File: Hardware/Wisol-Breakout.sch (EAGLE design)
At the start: 13 parts

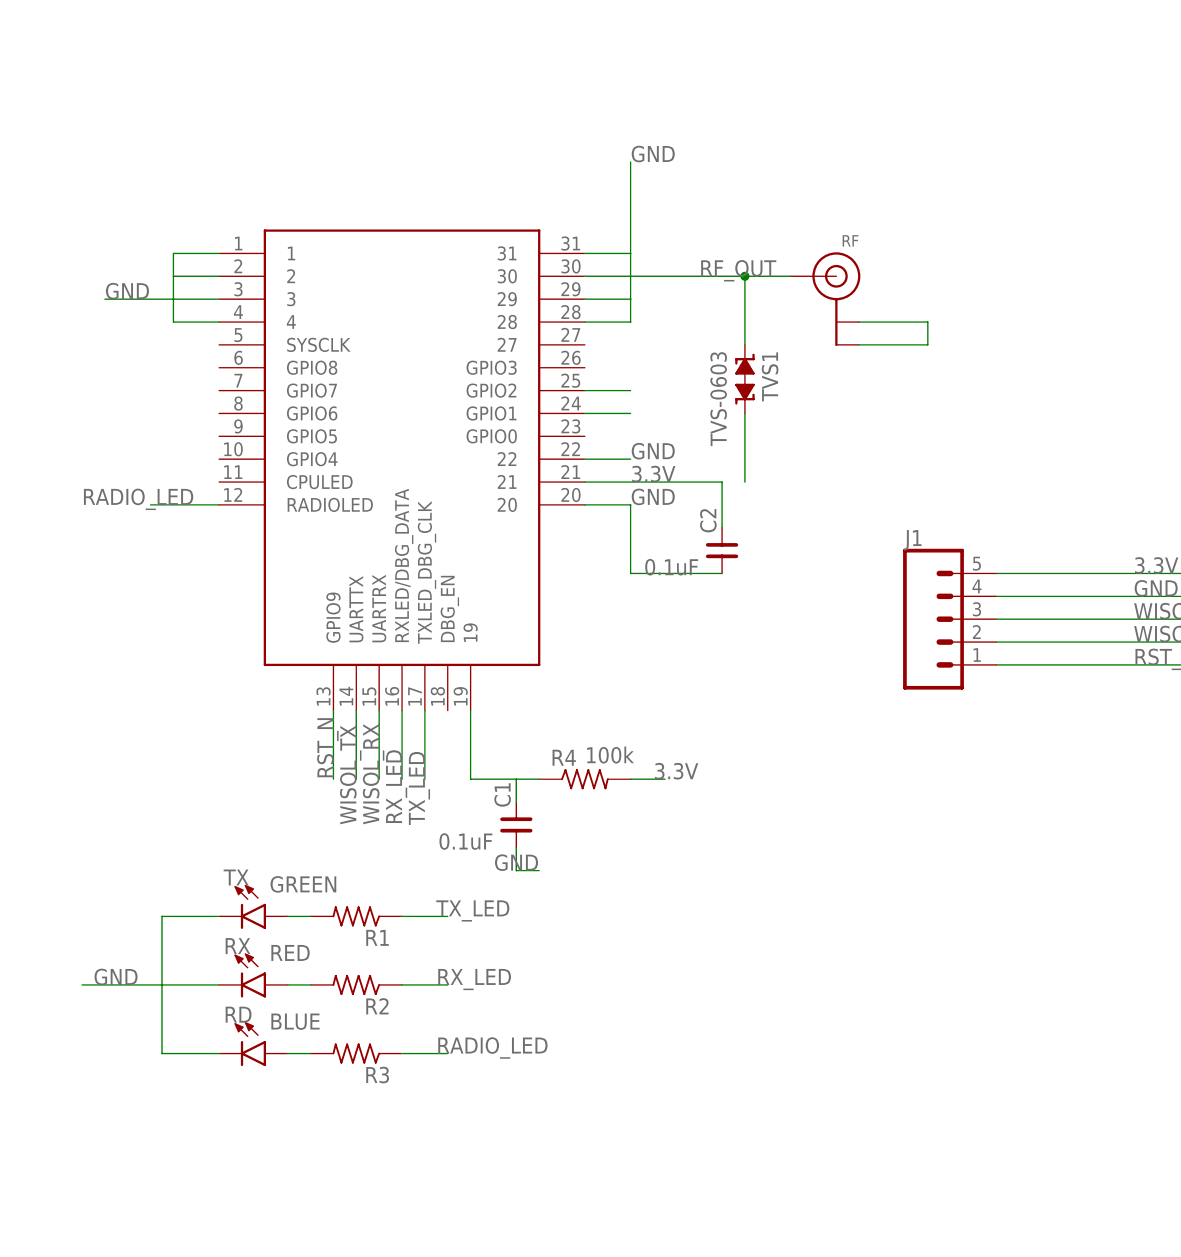
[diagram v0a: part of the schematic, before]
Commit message: Updated for Seeed PCB Assembly
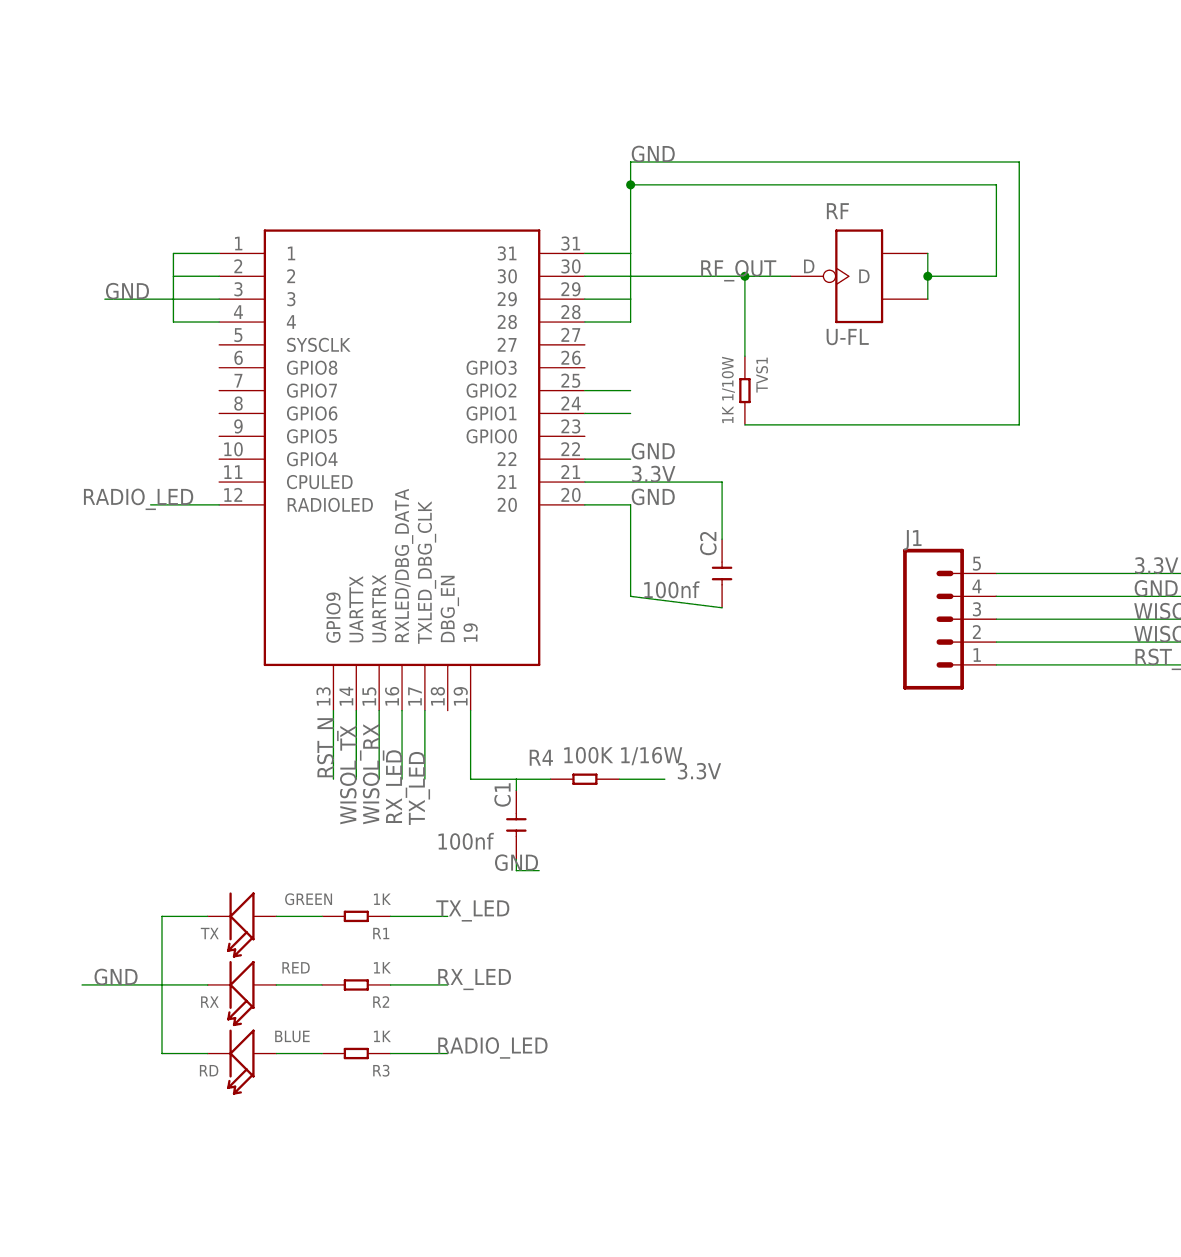
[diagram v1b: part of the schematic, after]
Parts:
- removed WSSFM10R2: WSSFM10R2/R4WSSFM10R2R4, SigfoxMod-RCZ1:WSSFM10R2/R4WSSFM10R2R4
- added WSSFM10R: WSSFM10RWSSFM10R2R4, WisolWSSFM10R:WSSFM10RWSSFM10R2R4
- C1, C2: value 0.1uF -> 100nf; device IoTthings:CNP-0402 -> Seeed-Capacitor:CERAMIC-100NF-25V-10%-X7R(0402)
- R1, R2, R3: value (none) -> 1K; device IoTthings:R-US_R0402 -> Seeed-Resistor:SMD-RES-1K-5%-1/16W(0402); MPN (none) -> RC0402FR-071KL
- R4: value 100k -> 100K 1/16W; device IoTthings:R-US_R0402 -> Seeed-Resistor:SMD-RES-100K-5%-1/16W(0402)
- RD: device IoTthings:LED-BLUE0603 -> Seeed-LED:SMD-LED-CLEAR-BLUE(0603)
- RF: value (none) -> U-FL; device IoTthings:ANTENNA_U.FL -> Seeed-Connector:ANTENNA-CONN-U-FL(3P)
- RX: device IoTthings:LED-RED0603 -> Seeed-LED:LED-SMD-RED-DIFFUSED(0603)
- TVS1: value TVS-0603 -> 1K 1/10W; device supressor:TVS-0603 -> Seeed-Fuse:SMD-ESD-CG0603MLC-05E
- TX: device IoTthings:LED-GREEN0603 -> Seeed-LED:SMD-LED-CLEAR-GREEN(0603)
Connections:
- net 3.3V: now also WSSFM10R.21; no longer WSSFM10R2.21
- net GND: now also RD.-, RF.GND1, RF.GND2, RX.-, TX.-, WSSFM10R.1, WSSFM10R.2, WSSFM10R.20, WSSFM10R.22, WSSFM10R.28, WSSFM10R.29, WSSFM10R.3, WSSFM10R.31, WSSFM10R.4; no longer RD.C, RF.GND@0, RF.GND@1, RX.C, TX.C, WSSFM10R2.1, WSSFM10R2.2, WSSFM10R2.20, WSSFM10R2.22, WSSFM10R2.28, WSSFM10R2.29, WSSFM10R2.3, WSSFM10R2.31, WSSFM10R2.4
- net GPIO1: now also WSSFM10R.GPIO1; no longer WSSFM10R2.GPIO1
- net GPIO2: now also WSSFM10R.GPIO2; no longer WSSFM10R2.GPIO2
- net N$1: now also WSSFM10R.19; no longer WSSFM10R2.19
- net N$2: now also TX.+; no longer TX.A
- net N$3: now also RX.+; no longer RX.A
- net N$4: now also RD.+; no longer RD.A
- net RADIO_LED: now also WSSFM10R.RADIOLED; no longer WSSFM10R2.RADIOLED
- net RF_OUT: now also RF.D, WSSFM10R.30; no longer RF.SIGNAL, WSSFM10R2.30
- net RST_N: now also WSSFM10R.GPIO9; no longer WSSFM10R2.GPIO9
- net RX_LED: now also WSSFM10R.RXLED/DBG_DATA; no longer WSSFM10R2.RXLED/DBG_DATA
- net TX_LED: now also WSSFM10R.TXLED_DBG_CLK; no longer WSSFM10R2.TXLED_DBG_CLK
- net WISOL_RX: now also WSSFM10R.UARTRX; no longer WSSFM10R2.UARTRX
- net WISOL_TX: now also WSSFM10R.UARTTX; no longer WSSFM10R2.UARTTX

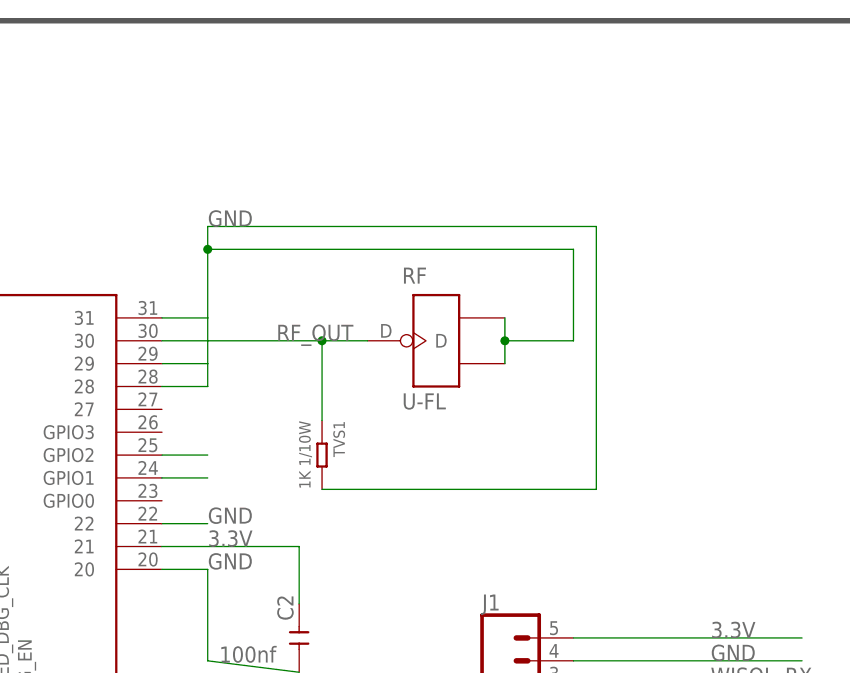
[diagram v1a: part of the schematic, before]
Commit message: Added RF inductor as recommended by Wisol H/W Design Guide
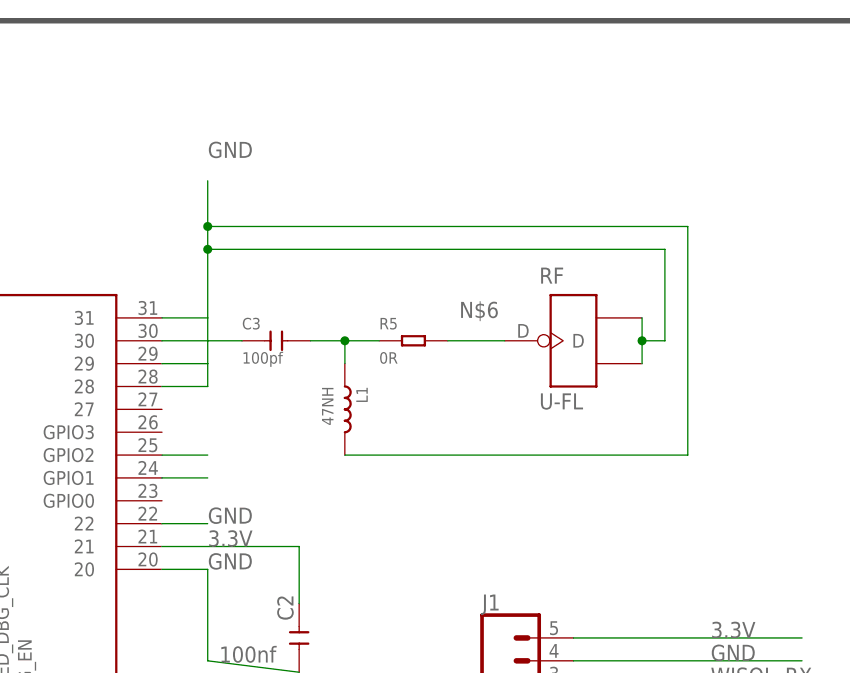
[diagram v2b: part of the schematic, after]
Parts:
- removed TVS1: 1K 1/10W, Seeed-Fuse:SMD-ESD-CG0603MLC-05E
- added C3: 100pf, Seeed-Capacitor:CERAMIC-100PF-50V-5%-NPO(0402)
- added L1: 47NH, Seeed-Inductor:SMD-INDUCTOR-15NH-5%-300MA(0402)
- added R5: 0R, Seeed-Resistor:SMD-RES-0R-5%-1/16W(0402)
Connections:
- new net N$5: C3.2, L1.1, R5.1
- new net N$6: R5.2, RF.D
- net GND: now also L1.2; no longer TVS1.2
- net RF_OUT: now also C3.1; no longer RF.D, TVS1.1
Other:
- moved on the sheet: RF
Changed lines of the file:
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@@
 <layer number="136" name="silktop" color="7" fill="1" visible="yes" active="yes"/>
 <layer number="137" name="silkbottom" color="7" fill="1" visible="yes" active="yes"/>
+<layer number="138" name="mbTest" color="7" fill="1" visible="yes" active="yes"/>
+<layer number="139" name="mtKeepout" color="7" fill="1" visible="yes" active="yes"/>
+<layer number="140" name="mbKeepout" color="7" fill="1" visible="yes" active="yes"/>
+<layer number="141" name="mtRestrict" color="7" fill="1" visible="yes" active="yes"/>
+<layer number="142" name="mbRestrict" color="7" fill="1" visible="yes" active="yes"/>
+<layer number="143" name="mvRestrict" color="7" fill="1" visible="yes" active="yes"/>
 <layer number="144" name="Drill_legend" color="7" fill="1" visible="yes" active="yes"/>
 <layer number="145" name="DrillLegend_01-16" color="7" fill="1" visible="yes" active="yes"/>
 <layer number="146" name="DrillLegend_01-20" color="7" fill="1" visible="yes" active="yes"/>
+<layer number="147" name="mMeasures" color="7" fill="1" visible="yes" active="yes"/>
+<layer number="148" name="mDocument" color="7" fill="1" visible="yes" active="yes"/>
+<layer number="149" name="mReference" color="7" fill="1" visible="yes" active="yes"/>
 <layer number="150" name="Notes" color="7" fill="1" visible="no" active="yes"/>
 <layer number="151" name="HeatSink" color="7" fill="1" visible="yes" active="yes"/>
@@
 <layer number="166" name="AntennaArea" color="7" fill="1" visible="yes" active="yes"/>
 <layer number="168" name="4mmHeightArea" color="7" fill="1" visible="yes" active="yes"/>
+<layer number="191" name="mNets" color="7" fill="1" visible="yes" active="yes"/>
+<layer number="192" name="mBusses" color="7" fill="1" visible="yes" active="yes"/>
+<layer number="193" name="mPins" color="7" fill="1" visible="yes" active="yes"/>
+<layer number="194" name="mSymbols" color="7" fill="1" visible="yes" active="yes"/>
+<layer number="195" name="mNames" color="7" fill="1" visible="yes" active="yes"/>
+<layer number="196" name="mValues" color="7" fill="1" visible="yes" active="yes"/>
 <layer number="199" name="Contour" color="7" fill="1" visible="no" active="yes"/>
 <layer number="200" name="200bmp" color="7" fill="1" visible="yes" active="yes"/>
@@
 <part name="R4" library="Seeed-Resistor" library_urn="urn:adsk.eagle:library:474" deviceset="SMD-RES-100K-5%-1/16W(0402)" device="" package3d_urn="urn:adsk.eagle:package:32792/1" value="100K 1/16W"/>
 <part name="C1" library="Seeed-Capacitor" library_urn="urn:adsk.eagle:library:464" deviceset="CERAMIC-100NF-25V-10%-X7R(0402)" device="" package3d_urn="urn:adsk.eagle:package:32379/1" value="100nf"/>
-<part name="TVS1" library="Seeed-Fuse" library_urn="urn:adsk.eagle:library:469" deviceset="SMD-ESD-CG0603MLC-05E" device="" package3d_urn="urn:adsk.eagle:package:32546/1" value="1K 1/10W"/>
 <part name="C2" library="Seeed-Capacitor" library_urn="urn:adsk.eagle:library:464" deviceset="CERAMIC-100NF-25V-10%-X7R(0402)" device="" package3d_urn="urn:adsk.eagle:package:32379/1" value="100nf"/>
 <part name="J1" library="SparkFun-Connectors" deviceset="CONN_05" device=""/>
@@
 <part name="TX" library="Seeed-LED" library_urn="urn:adsk.eagle:library:472" deviceset="SMD-LED-CLEAR-GREEN(0603)" device="" package3d_urn="urn:adsk.eagle:package:32743/1" value="GREEN"/>
 <part name="RF" library="Seeed-Connector" library_urn="urn:adsk.eagle:library:478" deviceset="ANTENNA-CONN-U-FL(3P)" device="" package3d_urn="urn:adsk.eagle:package:33122/1" value="U-FL"/>
+<part name="L1" library="Seeed-Inductor" deviceset="SMD-INDUCTOR-15NH-5%-300MA(0402)" device="" value="47NH">
+<attribute name="MPN" value="LQW15AN47NJ00D"/>
+</part>
+<part name="C3" library="Seeed-Capacitor" deviceset="CERAMIC-100PF-50V-5%-NPO(0402)" device="" value="100pf"/>
+<part name="R5" library="Seeed-Resistor" deviceset="SMD-RES-0R-5%-1/16W(0402)" device="" value="0R"/>
 </parts>
 <sheets>
@@
 <attribute name="VALUE" x="111.76" y="65.0875" size="1.778" layer="96" rot="R180"/>
 </instance>
-<instance part="TVS1" gate="G$1" x="139.7" y="114.3" rot="R270"/>
 <instance part="C2" gate="G$1" x="137.16" y="93.98" smashed="yes" rot="R90">
 <attribute name="NAME" x="136.525" y="95.885" size="1.778" layer="95" rot="R90"/>
@@
 <attribute name="VALUE" x="93.98" y="58.42" size="1.27" layer="96" ratio="10" rot="R180"/>
 </instance>
-<instance part="RF" gate="G$1" x="152.4" y="127"/>
+<instance part="RF" gate="G$1" x="167.64" y="127"/>
+<instance part="L1" gate="G$1" x="142.24" y="119.38" rot="R270"/>
+<instance part="C3" gate="G$1" x="134.62" y="127"/>
+<instance part="R5" gate="G$1" x="149.86" y="127"/>
 </instances>
 <busses>
@@
 <wire x1="127" y1="121.92" x2="127" y2="124.46" width="0.1524" layer="91"/>
 <wire x1="127" y1="129.54" x2="127" y2="137.16" width="0.1524" layer="91"/>
-<label x="127" y="139.7" size="1.778" layer="95"/>
+<label x="127" y="147.32" size="1.778" layer="95"/>
 <pinref part="RF" gate="G$1" pin="GND1"/>
 <pinref part="RF" gate="G$1" pin="GND2"/>
 <wire x1="127" y1="137.16" x2="127" y2="139.7" width="0.1524" layer="91"/>
-<wire x1="160.02" y1="129.54" x2="160.02" y2="127" width="0.1524" layer="91"/>
-<wire x1="160.02" y1="127" x2="160.02" y2="124.46" width="0.1524" layer="91"/>
-<wire x1="160.02" y1="127" x2="167.64" y2="127" width="0.1524" layer="91"/>
-<junction x="160.02" y="127"/>
-<wire x1="167.64" y1="127" x2="167.64" y2="137.16" width="0.1524" layer="91"/>
-<wire x1="167.64" y1="137.16" x2="127" y2="137.16" width="0.1524" layer="91"/>
+<wire x1="127" y1="139.7" x2="127" y2="144.78" width="0.1524" layer="91"/>
+<wire x1="175.26" y1="129.54" x2="175.26" y2="127" width="0.1524" layer="91"/>
+<wire x1="175.26" y1="127" x2="175.26" y2="124.46" width="0.1524" layer="91"/>
+<wire x1="175.26" y1="127" x2="177.8" y2="127" width="0.1524" layer="91"/>
+<junction x="175.26" y="127"/>
+<wire x1="177.8" y1="127" x2="177.8" y2="137.16" width="0.1524" layer="91"/>
+<wire x1="177.8" y1="137.16" x2="127" y2="137.16" width="0.1524" layer="91"/>
 <junction x="127" y="137.16"/>
-<pinref part="TVS1" gate="G$1" pin="2"/>
-<wire x1="139.7" y1="110.49" x2="170.18" y2="110.49" width="0.1524" layer="91"/>
-<wire x1="170.18" y1="110.49" x2="170.18" y2="139.7" width="0.1524" layer="91"/>
-<wire x1="170.18" y1="139.7" x2="127" y2="139.7" width="0.1524" layer="91"/>
+<pinref part="L1" gate="G$1" pin="2"/>
+<wire x1="142.24" y1="114.3" x2="180.34" y2="114.3" width="0.1524" layer="91"/>
+<wire x1="180.34" y1="114.3" x2="180.34" y2="139.7" width="0.1524" layer="91"/>
+<wire x1="180.34" y1="139.7" x2="127" y2="139.7" width="0.1524" layer="91"/>
+<junction x="127" y="139.7"/>
 </segment>
 <segment>
@@
 <segment>
 <pinref part="WSSFM10R" gate="G$1" pin="30"/>
-<label x="134.62" y="127" size="1.778" layer="95"/>
-<wire x1="139.7" y1="127" x2="121.92" y2="127" width="0.1524" layer="91"/>
-<wire x1="144.78" y1="127" x2="139.7" y2="127" width="0.1524" layer="91"/>
-<pinref part="TVS1" gate="G$1" pin="1"/>
-<wire x1="139.7" y1="118.11" x2="139.7" y2="127" width="0.1524" layer="91"/>
-<junction x="139.7" y="127"/>
-<pinref part="RF" gate="G$1" pin="D"/>
+<pinref part="C3" gate="G$1" pin="1"/>
+<wire x1="121.92" y1="127" x2="130.81" y2="127" width="0.1524" layer="91"/>
 </segment>
 </net>
@@
 </segment>
 </net>
+<net name="N$5" class="0">
+<segment>
+<pinref part="C3" gate="G$1" pin="2"/>
+<pinref part="R5" gate="G$1" pin="1"/>
+<wire x1="138.43" y1="127" x2="142.24" y2="127" width="0.1524" layer="91"/>
+<pinref part="L1" gate="G$1" pin="1"/>
+<wire x1="142.24" y1="127" x2="146.05" y2="127" width="0.1524" layer="91"/>
+<wire x1="142.24" y1="124.46" x2="142.24" y2="127" width="0.1524" layer="91"/>
+<junction x="142.24" y="127"/>
+</segment>
+</net>
+<net name="N$6" class="0">
+<segment>
+<pinref part="RF" gate="G$1" pin="D"/>
+<pinref part="R5" gate="G$1" pin="2"/>
+<wire x1="153.67" y1="127" x2="160.02" y2="127" width="0.1524" layer="91"/>
+<label x="154.94" y="129.54" size="1.778" layer="95"/>
+</segment>
+</net>

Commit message: Added revision
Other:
- note added: "3 Jul 2018"
- note added: "Note: This board layout was designed for Wisol WSSFM10R2 and R4, which have a longer footprint. Wisol WSSFM10R1 and R3 have a shorter footprint (the top part is truncated). All pins and PCB components remain the same."
- note added: "Wisol WSSFM10R"
- note added: "luppy@appkaki.com"
- note removed: "05/04/2017"
- note removed: "SeaSlugLabs"
- note removed: "Wisol WSSFM10R2"
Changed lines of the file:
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@@
 <wire x1="269.24" y1="5.08" x2="269.24" y2="-2.54" width="0.6096" layer="97"/>
 <wire x1="269.24" y1="-2.54" x2="246.38" y2="-2.54" width="0.6096" layer="97"/>
-<text x="223.52" y="27.94" size="5.08" layer="97">SeaSlugLabs</text>
+<text x="217.932" y="28.956" size="3.81" layer="97">luppy@appkaki.com</text>
 <wire x1="246.38" y1="-2.54" x2="213.36" y2="-2.54" width="0.6096" layer="97"/>
 <wire x1="213.36" y1="-2.54" x2="180.34" y2="-2.54" width="0.6096" layer="97"/>
@@
 <wire x1="213.36" y1="25.4" x2="213.36" y2="35.56" width="0.6096" layer="97"/>
 <wire x1="213.36" y1="35.56" x2="269.24" y2="35.56" width="0.6096" layer="97"/>
-<text x="220.98" y="17.78" size="3.81" layer="97">Wisol WSSFM10R2</text>
+<text x="219.456" y="17.78" size="3.81" layer="97">Wisol WSSFM10R</text>
 <text x="251.46" y="0" size="2.54" layer="97">REV A</text>
 <wire x1="213.36" y1="25.4" x2="213.36" y2="5.08" width="0.6096" layer="97"/>
@@
 <wire x1="246.38" y1="-2.54" x2="246.38" y2="5.08" width="0.6096" layer="97"/>
 <wire x1="213.36" y1="5.08" x2="213.36" y2="-2.54" width="0.6096" layer="97"/>
-<text x="226.06" y="10.16" size="3.81" layer="97">Sigfox Breakout</text>
+<text x="223.774" y="10.16" size="3.81" layer="97">Sigfox Breakout</text>
 <text x="187.96" y="2.54" size="1.778" layer="97">Release Date</text>
 <wire x1="213.36" y1="5.08" x2="180.34" y2="5.08" width="0.6096" layer="97"/>
 <wire x1="180.34" y1="5.08" x2="180.34" y2="-2.54" width="0.6096" layer="97"/>
-<text x="187.96" y="0" size="1.778" layer="97">05/04/2017</text>
+<text x="187.96" y="0" size="1.778" layer="97">3 Jul 2018</text>
 <text x="223.52" y="2.54" size="1.778" layer="97">Rev Date</text>
-<text x="223.52" y="0" size="1.778" layer="97">05/04/2017</text>
+<text x="223.52" y="0" size="1.778" layer="97">3 Jul 2018</text>
+<wire x1="86.36" y1="134.62" x2="116.84" y2="134.62" width="0.1524" layer="97"/>
+<wire x1="116.84" y1="134.62" x2="116.84" y2="147.32" width="0.1524" layer="97"/>
+<wire x1="116.84" y1="147.32" x2="86.36" y2="147.32" width="0.1524" layer="97"/>
+<wire x1="86.36" y1="147.32" x2="86.36" y2="134.62" width="0.1524" layer="97"/>
+<text x="87.63" y="136.652" size="1.016" layer="97">Note: This board layout was designed
+for Wisol WSSFM10R2 and R4, which
+have a longer footprint. Wisol WSSFM10R1
+and R3 have a shorter footprint (the
+top part is truncated). All pins and
+PCB components remain the same.</text>
 </plain>
 <instances>
@@
 </drawing>
 <compatibility>
+<note version="6.3" minversion="6.2.2" severity="warning">
+Since Version 6.2.2 text objects can contain more than one line,
+which will not be processed correctly with this version.
+</note>
 <note version="8.2" severity="warning">
 Since Version 8.2, EAGLE supports online libraries. The ids
